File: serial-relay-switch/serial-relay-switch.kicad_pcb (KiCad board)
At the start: 2 copper layers, 41.9 x 31.8 mm, 58 parts, among them J10 Conn_01x01, J11 Conn_01x01, J12 Conn_01x01, J13 Conn_01x01, J14 Conn_01x01, J15 Conn_01x01, J16 Conn_01x01, J17 Conn_01x01, J18 Conn_01x01, J2 2501551-4, J3 Conn_01x01, J4 Conn_01x01, J5 Conn_01x01, J6 Conn_01x01, J7 Conn_01x01, J8 Conn_01x01, J9 Conn_01x01, U1 74LS166, U2 ISL8488E, U3 74LVC1G08, U4 ISL8488E

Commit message: [rs] Mostly complete preliminary PCB placement
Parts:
- removed J12, J13, J14, J3: Conn_01x01, CUSTOM:Pin_D1.0mm
- removed R10, R11, R9: 1k, Resistor_SMD:R_0603_1608Metric
- removed R12, R13, R14, R15, R16, R17, R18, R19, R20, R23, R26: 10k, Resistor_SMD:R_0603_1608Metric
- removed R29: 120, Resistor_SMD:R_0603_1608Metric
- added C10: 0.1uF, Capacitor_SMD:C_0603_1608Metric, F.Cu at (153.9, 6.39)
- added C7: 0.1uF, Capacitor_SMD:C_0603_1608Metric, F.Cu at (137.6, 1.97)
- added C8: 0.1uF, Capacitor_SMD:C_0603_1608Metric, F.Cu at (132.5, 9.59)
- added C9: 0.1uF, Capacitor_SMD:C_0603_1608Metric, F.Cu at (128.4, 0.70)
- added D1: 1N4148, Diode_SMD:D_SOD-123F, F.Cu at (47.9, 67.9)
- added D2: LED, LED_SMD:LED_0603_1608Metric, F.Cu at (56.1, 59.9)
- added D3: LED, LED_SMD:LED_0603_1608Metric, F.Cu at (147.5, 59.9)
- added D4: LED, LED_SMD:LED_0603_1608Metric, F.Cu at (86.5, 59.9)
- added D5: LED, LED_SMD:LED_0603_1608Metric, F.Cu at (117.0, 59.9)
- added D6: LED, LED_SMD:LED_0603_1608Metric, F.Cu at (71.3, 59.9)
- added D7: LED, LED_SMD:LED_0603_1608Metric, F.Cu at (101.8, 59.9)
- added D8: LED, LED_SMD:LED_0603_1608Metric, F.Cu at (132.3, 59.9)
- added D9: LED, LED_SMD:LED_0603_1608Metric, F.Cu at (162.7, 59.9)
- added H4: MountingHole, MountingHole:MountingHole_3.2mm_M3, F.Cu at (41.6, 46.4)
- added J1: Screw_Terminal_01x01, CUSTOM:8195, F.Cu at (45.4, 82.0)
- added J19: Screw_Terminal_01x01, CUSTOM:8195, F.Cu at (150.8, 99.8)
- added J20: Screw_Terminal_01x01, CUSTOM:8195, F.Cu at (166.0, 99.8)
- added J21: Conn_01x01, CUSTOM:Pin_D1.0mm, F.Cu at (149.9, 43.1)
- added K1: G2RL-1-E, Relay_THT:Relay_SPDT_Omron_G2RL-1-E, F.Cu at (55.7, 64.9)
- added K2: G2RL-1-E, Relay_THT:Relay_SPDT_Omron_G2RL-1-E, F.Cu at (86.2, 64.9)
- added K3: G2RL-1-E, Relay_THT:Relay_SPDT_Omron_G2RL-1-E, F.Cu at (116.6, 64.9)
- added K4: G2RL-1-E, Relay_THT:Relay_SPDT_Omron_G2RL-1-E, F.Cu at (70.9, 64.9)
- added K5: G2RL-1-E, Relay_THT:Relay_SPDT_Omron_G2RL-1-E, F.Cu at (101.4, 64.9)
- added K6: G2RL-1-E, Relay_THT:Relay_SPDT_Omron_G2RL-1-E, F.Cu at (131.9, 64.9)
- added K7: G2RL-1-E, Relay_THT:Relay_SPDT_Omron_G2RL-1-E, F.Cu at (147.1, 64.9)
- added K8: G2RL-1-E, Relay_THT:Relay_SPDT_Omron_G2RL-1-E, F.Cu at (162.4, 64.9)
- added PS1: IRM-10-5, Converter_ACDC:Converter_ACDC_MeanWell_IRM-10-xx_THT, F.Cu at (186.4, 87.1)
- added R30: 100k, Resistor_THT:R_Axial_DIN0414_L11.9mm_D4.5mm_P5.08mm_Vertical, F.Cu at (42.9, 72.6)
- added U10: SZNUD3124LT1G, Package_TO_SOT_SMD:SOT-23, F.Cu at (139.4, 59.9)
- added U11: SZNUD3124LT1G, Package_TO_SOT_SMD:SOT-23, F.Cu at (154.6, 59.9)
- added U12: SZNUD3124LT1G, Package_TO_SOT_SMD:SOT-23, F.Cu at (169.8, 59.9)
- added U13: 74HCT595, Package_SO:SOIC-16_3.9x9.9mm_P1.27mm, F.Cu at (113.0, 52.8)
- added U14: 74LVC1G32, Package_TO_SOT_SMD:SOT-23-5, F.Cu at (129.2, 9.59)
- added U15: 74LVC1G08, Package_TO_SOT_SMD:SOT-23-5, F.Cu at (135.4, 5.46)
- added U16: 74LVC1G04, Package_TO_SOT_SMD:SOT-23-5, F.Cu at (129.2, 4.51)
- added U17: 74LS163, Package_SO:SOIC-16_3.9x9.9mm_P1.27mm, F.Cu at (96.2, 49.7)
- added U6: SZNUD3124LT1G, Package_TO_SOT_SMD:SOT-23, F.Cu at (93.7, 59.9)
- added U7: SZNUD3124LT1G, Package_TO_SOT_SMD:SOT-23, F.Cu at (124.1, 59.9)
- added U8: SZNUD3124LT1G, Package_TO_SOT_SMD:SOT-23, F.Cu at (78.5, 59.9)
- added U9: SZNUD3124LT1G, Package_TO_SOT_SMD:SOT-23, F.Cu at (108.9, 59.9)
- C2: footprint Capacitor_SMD:C_1206_3216Metric -> Capacitor_THT:C_Radial_D8.0mm_H7.0mm_P3.50mm
- J10, J11, J15, J16, J4, J5, J6, J7, J8, J9: value Conn_01x01 -> Screw_Terminal_01x01; footprint CUSTOM:Pin_D1.0mm -> CUSTOM:8195
- R1: value 10k -> 1k; footprint Resistor_THT:R_Axial_DIN0204_L3.6mm_D1.6mm_P2.54mm_Vertical -> Resistor_SMD:R_0603_1608Metric
- R2: value 10k -> 1k
- U1: value 74LS166 -> H11L1; footprint Package_SO:Texas_DYY0016A_TSOT-23-16_2x4.2mm_P0.5mm -> Package_DIP:DIP-6_W10.16mm_LongPads
- U3: value 74LVC1G08 -> SZNUD3124LT1G; footprint Package_SO:TSOP-5_1.65x3.05mm_P0.95mm -> Package_TO_SOT_SMD:SOT-23
- moved H3 125.9 mm to (211.8, 46.4)
- moved LAY1 116.9 mm to (204.1, 46.4)
- moved H1 109.4 mm to (211.8, 104.8)
- moved J15 109.0 mm to (208.6, 71.8)
- moved C5 107.4 mm to (174.2, 4.51), turned to 0 degrees
- moved R24 106.7 mm to (157.9, 13.9), turned to 0 degrees
- moved R22 105.6 mm to (157.9, 11.4), turned to 0 degrees
- moved C4 104.5 mm to (149.8, 8.90), turned to 0 degrees
- moved C6 102.2 mm to (121.1, -0.57), turned to 0 degrees
- moved R25 100.2 mm to (157.9, 16.4), turned to 0 degrees
- moved R27 99.0 mm to (157.9, 18.9), turned to 0 degrees
- moved H2 96.7 mm to (41.6, 104.8)
- moved J16 94.2 mm to (196.5, 99.8), turned to 0 degrees
- moved R28 93.6 mm to (157.9, 21.4), turned to 0 degrees
- moved U1 93.6 mm to (42.9, 62.9), turned to 90 degrees
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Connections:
- J10 pad 1: Net-(J10-Pin_1) -> /OUT_D
- J11 pad 1: Net-(J11-Pin_1) -> /OUT_F
- J15 pad 1: +5V -> GND
- J16 pad 1: GND -> /NEUTRAL
- J17 pad 1: /LOADB -> /SCAN_IN
- J2 pad 12: /LOADB -> GND
- J2 pad 7: /SO_N -> /SI_N
- J2 pad 8: /SO_P -> /SI_P
- J4 pad 1: Net-(J4-Pin_1) -> /NEUTRAL
- J5 pad 1: Net-(J5-Pin_1) -> GND
- J6 pad 1: Net-(J6-Pin_1) -> /OUT_A
- J7 pad 1: Net-(J7-Pin_1) -> /OUT_C
- J8 pad 1: Net-(J8-Pin_1) -> /OUT_E
- J9 pad 1: Net-(J9-Pin_1) -> /OUT_B
- R1 pad 1: /SCAN_IN -> /CTL_A
- R1 pad 2: GND -> Net-(D2-A)
- R2 pad 1: Net-(R11-Pad2) -> /CTL_G
- R2 pad 2: GND -> Net-(D3-A)
- R22 pad 2: /LD_P -> /SI_P
- R25 pad 1: /LD_N -> /SI_N
- R27 pad 2: +5V -> /COUNT_RCO
- R28 pad 1: /LD_N -> /SI_N
- R28 pad 2: /LD_P -> /SI_P
- R3 pad 1: Net-(J3-Pin_1) -> /CTL_C
- R3 pad 2: /IN_A -> Net-(D4-A)
- R4 pad 1: Net-(J4-Pin_1) -> /CTL_E
- R4 pad 2: /IN_B -> Net-(D5-A)
- R5 pad 1: Net-(J5-Pin_1) -> /CTL_B
- R5 pad 2: /IN_C -> Net-(D6-A)
- R6 pad 1: Net-(J6-Pin_1) -> /CTL_D
- R6 pad 2: /IN_D -> Net-(D7-A)
- R7 pad 1: Net-(J7-Pin_1) -> /CTL_F
- R7 pad 2: /IN_E -> Net-(D8-A)
- R8 pad 1: Net-(J8-Pin_1) -> /CTL_H
- R8 pad 2: /IN_F -> Net-(D9-A)
- U1 pad 1: /SCAN_IN -> Net-(D1-K)
- U1 pad 2: /IN_A -> /NEUTRAL
- U1 pad 3: /IN_B -> unconnected-(U1-Pad3)
- U1 pad 4: /IN_C -> /CLK
- U1 pad 5: /IN_D -> GND
- U1 pad 6: GND -> +5V
- U2 pad 2: /LOADB -> /SCAN_IN
- U2 pad 3: /SCAN_OUT -> /LOAD
- U2 pad 5: /SO_P -> /LD_P
- U2 pad 6: /SO_N -> /LD_N
- U2 pad 7: /LD_N -> /SI_N
- U2 pad 8: /LD_P -> /SI_P
- U3 pad 1: Net-(R11-Pad2) -> /CTL_A
- U3 pad 2: Net-(U1-Qh) -> GND
- U3 pad 3: GND -> Net-(K1-PadA2)
- U4 pad 2: /CLK -> unconnected-(U4-RO-Pad2)
- U4 pad 3: GND -> /CLK
- U4 pad 5: unconnected-(U4-Y-Pad5) -> /CLK_P
- U4 pad 6: unconnected-(U4-Z-Pad6) -> /CLK_N
- U4 pad 7: /CLK_N -> unconnected-(U4-B-Pad7)
- U4 pad 8: /CLK_P -> unconnected-(U4-A-Pad8)
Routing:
- net /LOADB: track 46.6 -> 0.00 mm, vias 2 -> 0
- net +5V: track 38.0 -> 0.00 mm, vias 4 -> 0
- net GND: track 35.5 -> 0.00 mm, vias 20 -> 0
- net /CLK: track 34.8 -> 0.00 mm
- net /LD_P: track 19.2 -> 0.00 mm
- net /LD_N: track 18.0 -> 0.00 mm
- net /CLK_N: track 14.3 -> 0.00 mm
- net /IN_A: track 13.8 -> 0.00 mm
- net /IN_H: track 13.1 -> 0.00 mm
- net /CLK_P: track 12.0 -> 0.00 mm
- net /SCAN_OUT: track 11.6 -> 0.00 mm
- net /SO_P: track 11.3 -> 0.00 mm
- net /IN_B: track 10.8 -> 0.00 mm
- net Net-(R11-Pad2): track 10.5 -> 0.00 mm
- net /IN_C: track 10.0 -> 0.00 mm
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- removed copper zone on F.Cu, net +5V
- removed copper zone on B.Cu, net GND
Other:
- board size 41.9 x 31.8 mm -> 177.8 x 66 mm
- board text removed: "(+)"
- board text removed: "(-)"
- board text removed: "+"
- board text removed: "-"
- board text removed: "A"
- board text removed: "B"
- board text removed: "C"
- board text removed: "CLK"
- board text removed: "D"
- board text removed: "E"
- board text removed: "EN"
- board text removed: "F"
- board text removed: "G"
- board text removed: "H"
- board text removed: "LDB"
- board text removed: "SI"
- board text removed: "SO"

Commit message: [rs] New preliminary board layout
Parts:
- removed J15, J16: Screw_Terminal_01x01, CUSTOM:8195
- added H5: MountingHole, MountingHole:MountingHole_3.2mm_M3, F.Cu at (161.0, 54.0)
- K1, K2, K3, K4, K5, K6, K7, K8: footprint Relay_THT:Relay_SPDT_Omron_G2RL-1-E -> CUSTOM:Relay_SPDT_Omron_G2RL-1-E
- moved LAY1 160.4 mm to (52.4, 98.4)
- moved J5 156.2 mm to (52.4, 57.2), turned to -90 degrees
- moved J4 120.6 mm to (63.2, 99.8)
- moved PS1 115.8 mm to (70.6, 86.2)
- moved K3 39.8 mm to (154.6, 76.9)
- moved K8 39.8 mm to (200.3, 76.9)
- moved K1 39.8 mm to (93.7, 76.9)
- moved K4 39.8 mm to (108.9, 76.9)
- moved K5 39.8 mm to (139.4, 76.9)
- moved K2 39.8 mm to (124.1, 76.9)
- moved K6 39.8 mm to (169.8, 76.9)
- moved K7 39.8 mm to (185.1, 76.9)
- moved J1 37.5 mm to (78.4, 99.8), turned to 0 degrees
- moved D3 34.3 mm to (181.8, 61.2)
- moved J2 34.3 mm to (205.4, 55.8)
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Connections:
- D1 pad 1: Net-(D1-K) -> /NEUTRAL
- D1 pad 2: /NEUTRAL -> Net-(D1-A)
- R30 pad 2: Net-(D1-K) -> Net-(D1-A)
- U1 pad 1: Net-(D1-K) -> /NEUTRAL
- U1 pad 2: /NEUTRAL -> Net-(D1-A)
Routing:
- net /LINE: track 0.00 -> 31.7 mm
- net /NEUTRAL: track 0.00 -> 26.2 mm
- net Net-(D1-A): track 0.00 -> 10.4 mm
- added copper zone on B.Cu, net /LINE
- added copper zone on F.Cu, net /LINE
- added copper zone on B.Cu, net /NEUTRAL
- added copper zone on F.Cu, net /NEUTRAL
- added copper zone on B.Cu, net /OUT_A
- added copper zone on F.Cu, net /OUT_A
- added copper zone on B.Cu, net /OUT_B
- added copper zone on F.Cu, net /OUT_B
- added copper zone on B.Cu, net /OUT_C
- added copper zone on F.Cu, net /OUT_C
- added copper zone on B.Cu, net /OUT_D
- added copper zone on F.Cu, net /OUT_D
- added copper zone on B.Cu, net /OUT_E
- added copper zone on F.Cu, net /OUT_E
- added copper zone on B.Cu, net /OUT_F
- added copper zone on F.Cu, net /OUT_F
- added copper zone on B.Cu, net /OUT_G
- added copper zone on F.Cu, net /OUT_G
- added copper zone on B.Cu, net /OUT_H
- added copper zone on F.Cu, net /OUT_H
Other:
- board size 177.8 x 66 mm -> 170.2 x 66 mm

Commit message: [rs] Routing progress
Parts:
- moved C4 119.3 mm to (43.5, 62.9)
- moved R24 57.7 mm to (201.7, 51.5), turned to -90 degrees
- moved C10 51.0 mm to (171.6, 54.2), turned to -90 degrees
- moved U16 50.2 mm to (106.5, 49.3)
- moved C7 50.2 mm to (114.9, 46.7)
- moved C8 50.2 mm to (109.8, 54.4)
- moved C9 50.2 mm to (105.7, 45.5)
- moved U14 50.2 mm to (106.5, 54.4)
- moved U15 50.2 mm to (112.7, 50.2)
- moved C6 50.2 mm to (100.4, 45.1)
- moved C3 47.9 mm to (130.5, 50.2)
- moved C5 43.4 mm to (171.4, 47.8), turned to -90 degrees
- moved R22 39.7 mm to (178.7, 45.1)
- moved H5 38.1 mm to (122.9, 54.0)
- moved U2 35.8 mm to (176.2, 49.0)
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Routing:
- net /CTL_H: track 0.00 -> 63.8 mm
- net /CTL_A: track 0.00 -> 57.1 mm
- net /CTL_G: track 0.00 -> 47.7 mm
- net /CTL_B: track 0.00 -> 36.2 mm
- net /CTL_F: track 0.00 -> 34.4 mm
- net GND: track 0.00 -> 34.1 mm, vias 0 -> 23
- net /CTL_C: track 0.00 -> 22.5 mm
- net /CLK_N: track 0.00 -> 21.3 mm, vias 0 -> 1
- net /CTL_E: track 0.00 -> 19.7 mm
- net /CLK_P: track 0.00 -> 19.0 mm
- net /CTL_D: track 0.00 -> 10.6 mm
- net /SI_N: track 0.00 -> 7.85 mm
- net Net-(J2-LED1+): track 0.00 -> 7.12 mm
- net /SI_P: track 0.00 -> 5.48 mm
- net +5V: track 0.00 -> 4.89 mm
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- added copper zone on F.Cu, net +5V
- added copper zone on B.Cu, net GND
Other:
- outline, holes or cut-outs redrawn

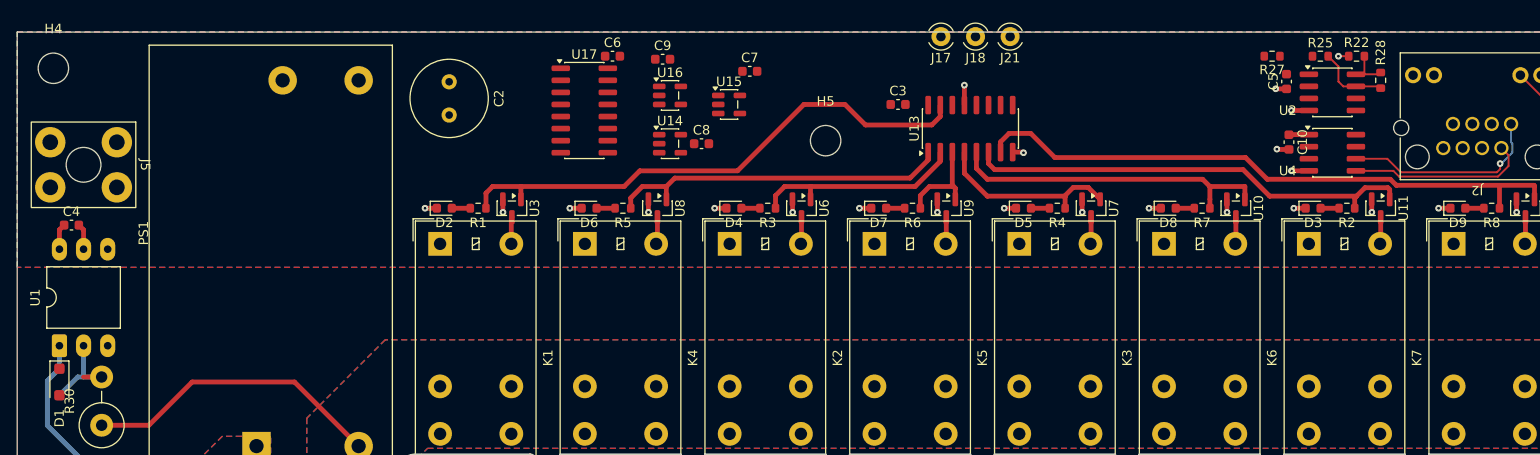
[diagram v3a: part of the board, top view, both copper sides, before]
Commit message: [rs] Routed, save for the pesky "Unrouted 1"
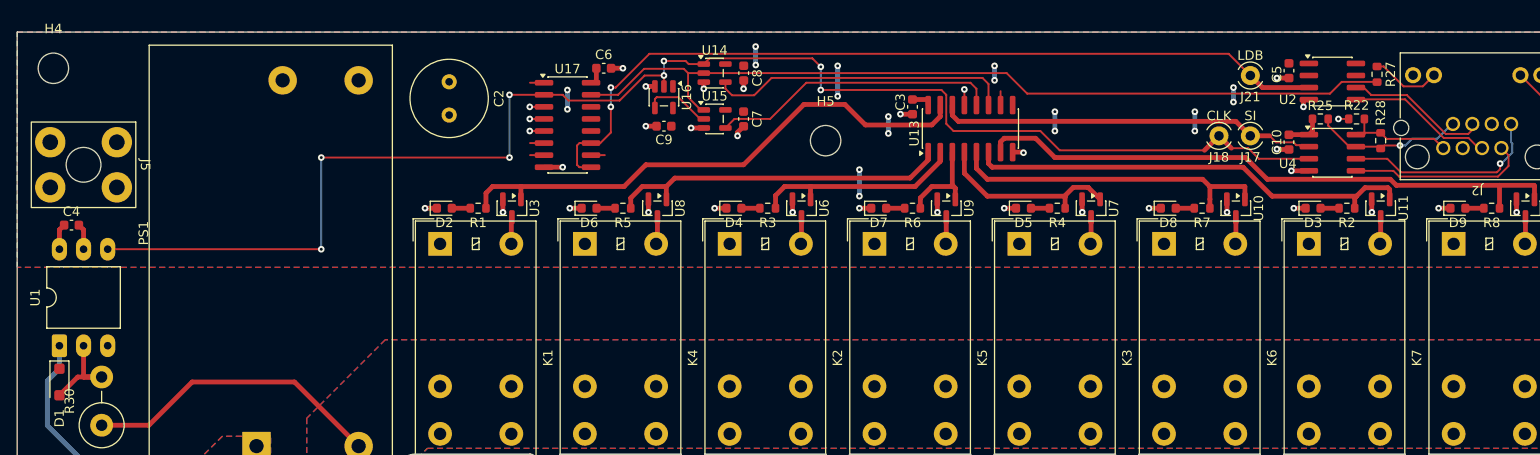
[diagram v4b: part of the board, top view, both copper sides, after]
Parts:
- moved J17 34.2 mm to (167.6, 53.5)
- moved J18 27.7 mm to (164.3, 53.5)
- moved J21 25.6 mm to (167.6, 47.2)
- moved R27 11.2 mm to (180.9, 47.1), turned to -90 degrees
- moved U14 8.79 mm to (111.2, 46.9)
- moved C8 8.66 mm to (114.2, 46.9), turned to -90 degrees
- moved C9 7.05 mm to (105.8, 52.5), turned to 180 degrees
- moved R22 6.60 mm to (178.7, 51.8)
- moved R25 6.60 mm to (174.9, 51.8)
- moved R28 6.35 mm to (181.3, 54.0)
- moved C7 5.06 mm to (114.2, 51.8), turned to -90 degrees
- moved U17 2.33 mm to (95.7, 52.4)
- moved U15 2.16 mm to (111.2, 51.8)
- moved C6 1.57 mm to (99.5, 46.4)
- moved C3 1.55 mm to (132.0, 50.5), turned to -90 degrees
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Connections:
- net /LOAD renamed /LOADB
- U14 pad 1: /COUNT_RCO -> /CLK
- U14 pad 2: /CLK -> /COUNT_RCO
- U15 pad 1: /CLKB -> /COUNT_RCO
- U15 pad 2: /COUNT_RCO -> /CLKB
- U17 pad 10: GND -> +5V
- U17 pad 7: GND -> +5V
- U2 pad 2: /SCAN_IN -> unconnected-(U2-RO-Pad2)
- U2 pad 7: /SI_N -> unconnected-(U2-B-Pad7)
- U2 pad 8: /SI_P -> unconnected-(U2-A-Pad8)
- U4 pad 2: unconnected-(U4-RO-Pad2) -> /SCAN_IN
- U4 pad 7: unconnected-(U4-B-Pad7) -> /SI_N
- U4 pad 8: unconnected-(U4-A-Pad8) -> /SI_P
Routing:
- net /CLK: track 0.00 -> 155.9 mm, vias 0 -> 8
- net /COUNT_RCO: track 0.00 -> 90.2 mm
- net /LOADB: track 0.00 -> 88.9 mm, vias 0 -> 2
- net /SCAN_IN: track 0.00 -> 40.0 mm
- net /RECEIVE_CLK: track 0.00 -> 31.9 mm
- net +5V: track 4.89 -> 36.4 mm, vias 0 -> 18
- net /OUTPUT_UPDATE: track 0.00 -> 30.4 mm
- net /LD_P: track 0.00 -> 15.4 mm
- net /LD_N: track 0.00 -> 15.1 mm
- net GND: track 34.1 -> 48.6 mm, vias 23 -> 35
- net /SI_N: track 7.85 -> 15.9 mm, vias 0 -> 1
- net Net-(J2-LED2-): track 0.00 -> 7.35 mm
- net /CLKB: track 0.00 -> 7.12 mm
- net /SI_P: track 5.48 -> 12.5 mm
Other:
- board text added: "CLK"
- board text added: "LDB"
- board text added: "SI"

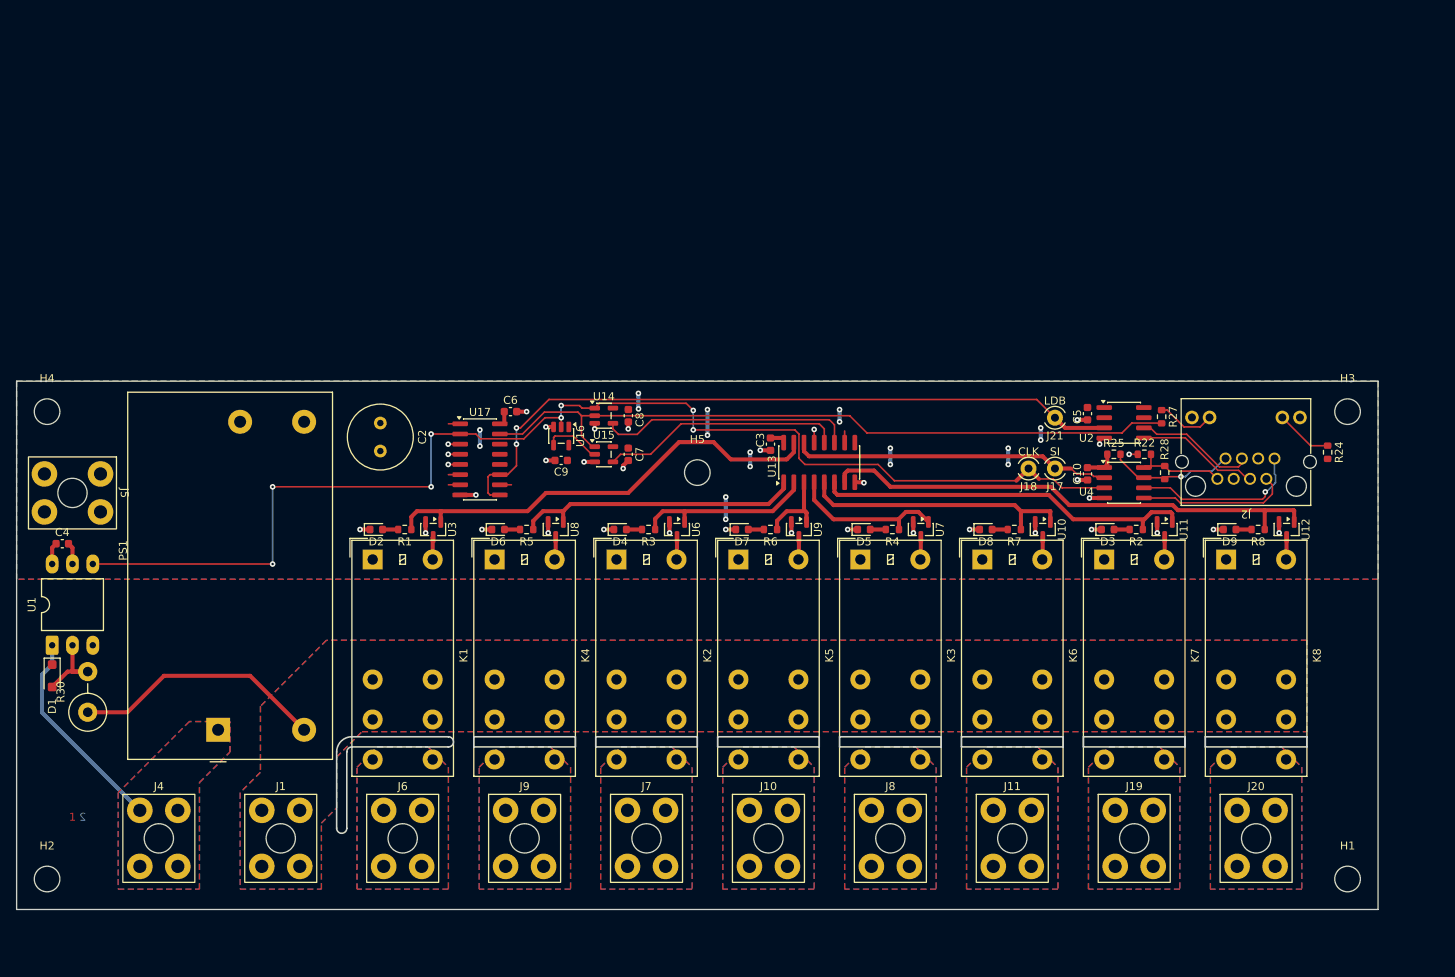
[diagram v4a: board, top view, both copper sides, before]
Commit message: [rs] Silk cleanup
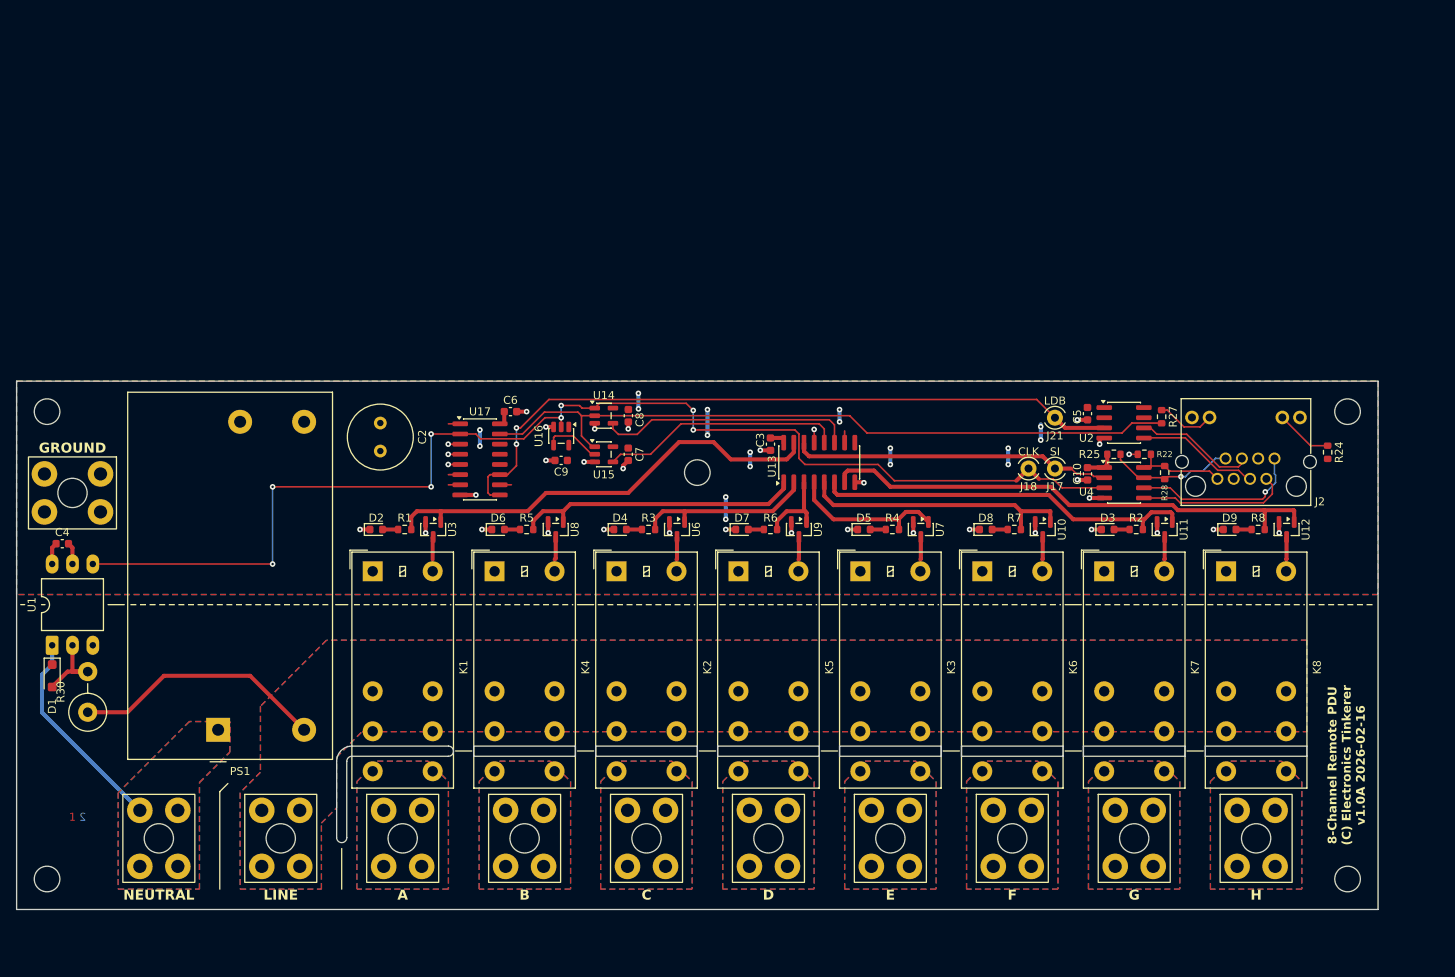
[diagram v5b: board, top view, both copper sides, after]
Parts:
- moved K1 1.47 mm to (86.0, 78.4)
- moved K2 1.47 mm to (116.5, 78.4)
- moved K3 1.47 mm to (147.0, 78.4)
- moved K4 1.47 mm to (101.3, 78.4)
- moved K5 1.47 mm to (131.8, 78.4)
- moved K6 1.47 mm to (162.2, 78.4)
- moved K7 1.47 mm to (177.5, 78.4)
- moved K8 1.47 mm to (192.7, 78.4)
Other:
- outline, holes or cut-outs redrawn
- board text added: "8-Channel Remote PDU (C) Electronics Tinkerer v1.0A 2026-02-16"
- board text added: "A"
- board text added: "B"
- board text added: "C"
- board text added: "D"
- board text added: "E"
- board text added: "F"
- board text added: "G"
- board text added: "GROUND"
- board text added: "H"
- board text added: "LINE"
- board text added: "NEUTRAL"
